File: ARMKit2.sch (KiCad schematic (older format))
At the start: 37 parts, among them P1 CONN_01X06, P2 CONN_01X32, P3 CONN_01X32, P4 USB_B, SW1 SW_PUSH, SW2 SW_PUSH, U1 STM32F405RG, U2 LT1761, Y1 Crystal, Y2 Crystal

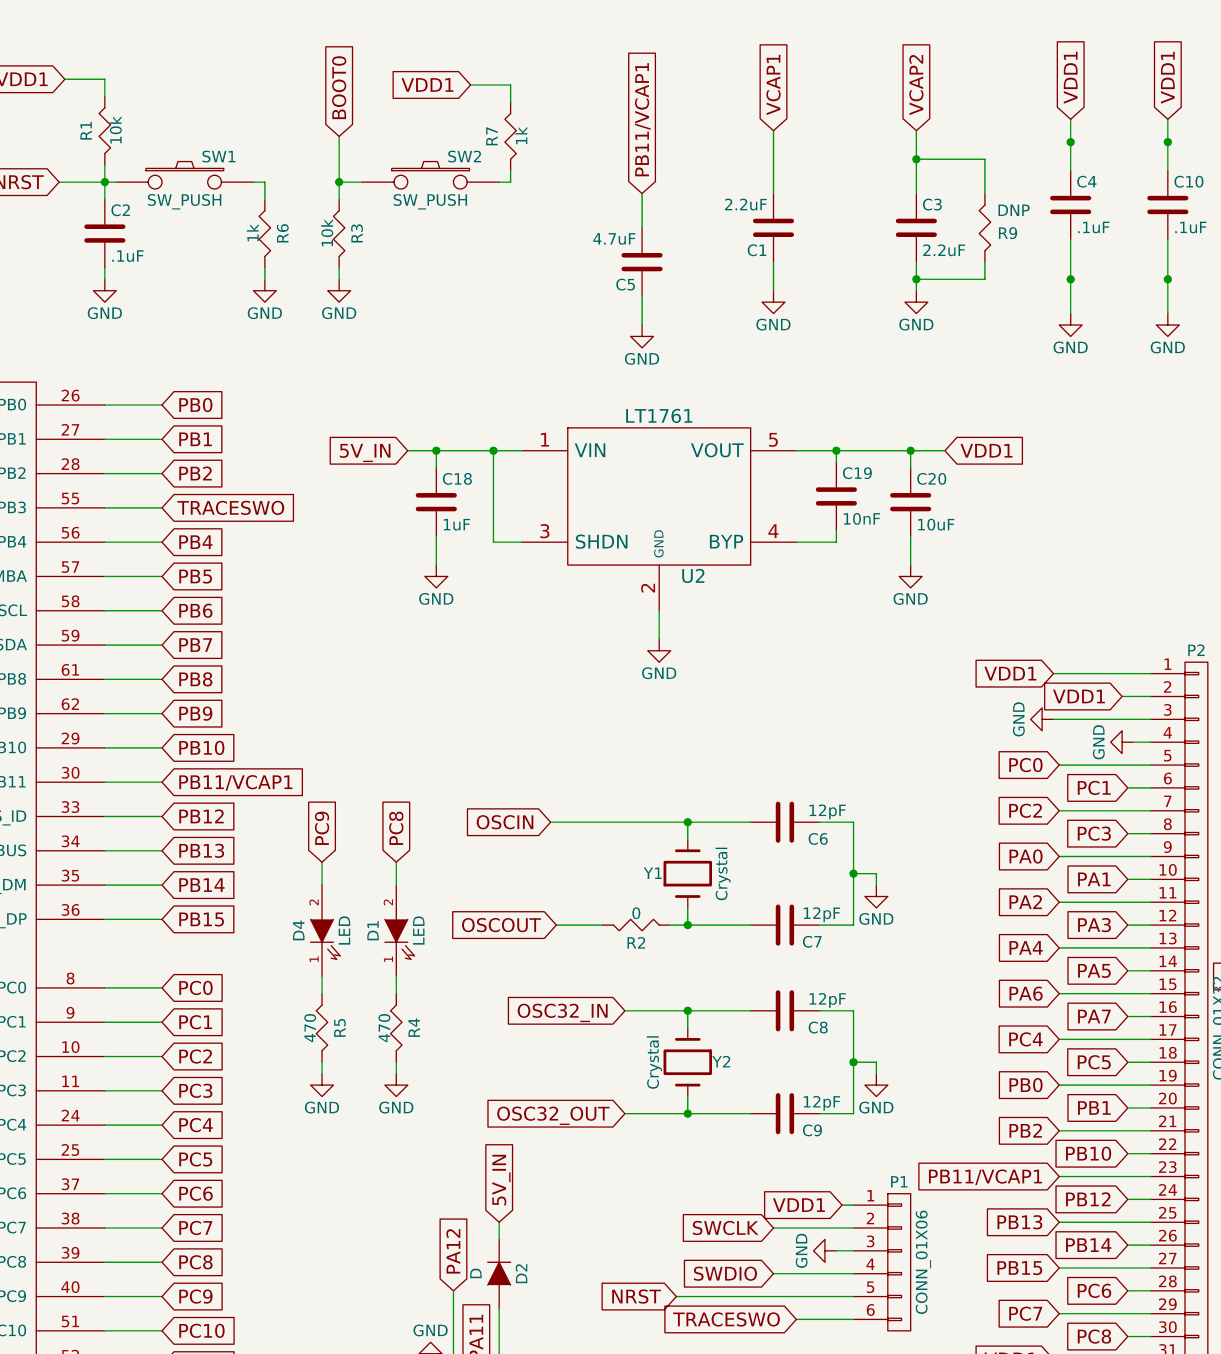
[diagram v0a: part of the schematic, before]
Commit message: Moved outline, can direct upload to OSHPark
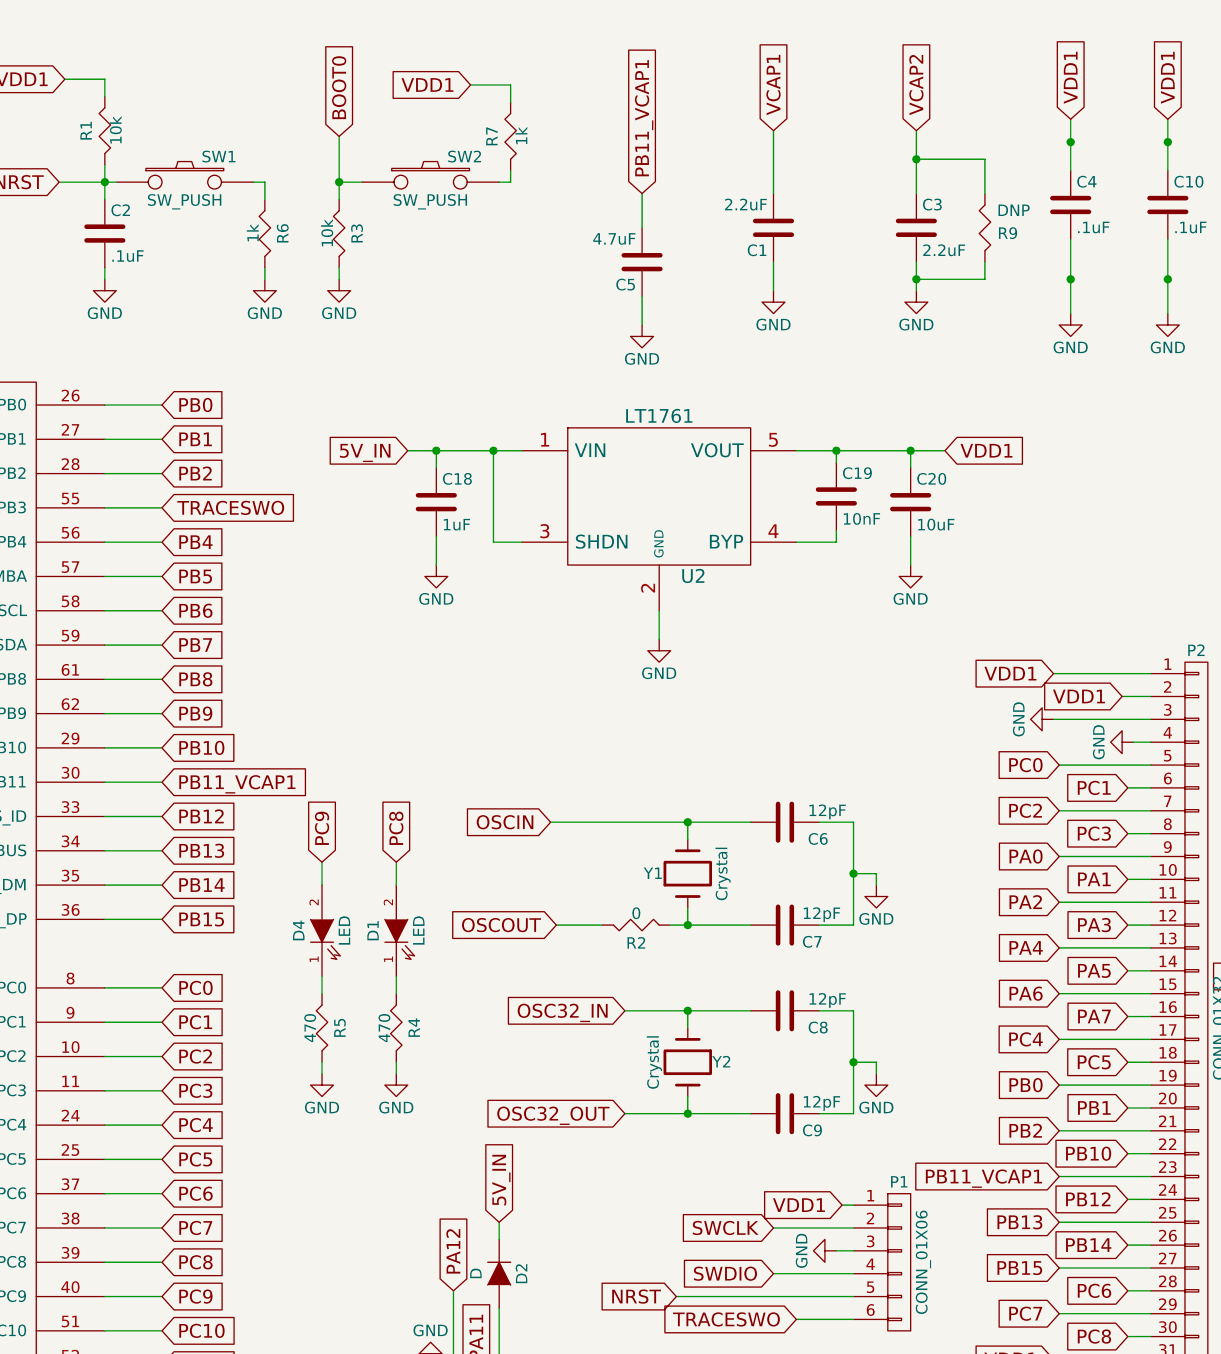
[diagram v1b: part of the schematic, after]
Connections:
- net PB11/VCAP1 renamed PB11_VCAP1
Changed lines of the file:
@@
 	4950 4350 5200 4350
 Text GLabel 5200 3750 2    60   Input ~ 0
-PB11/VCAP1
+PB11_VCAP1
 Text GLabel 5200 3900 2    60   Input ~ 0
 PB12
@@
 	9525 5875 9125 5875
 Text GLabel 9125 5475 0    60   Input ~ 0
-PB11/VCAP1
+PB11_VCAP1
 Text GLabel 9425 5575 0    60   Input ~ 0
 PB12
@@
 Connection ~ 8500 1550
 Text GLabel 7300 1175 1    60   Input ~ 0
-PB11/VCAP1
+PB11_VCAP1
 $Comp
 L C C5
